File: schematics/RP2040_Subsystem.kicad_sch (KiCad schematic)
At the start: 0 parts

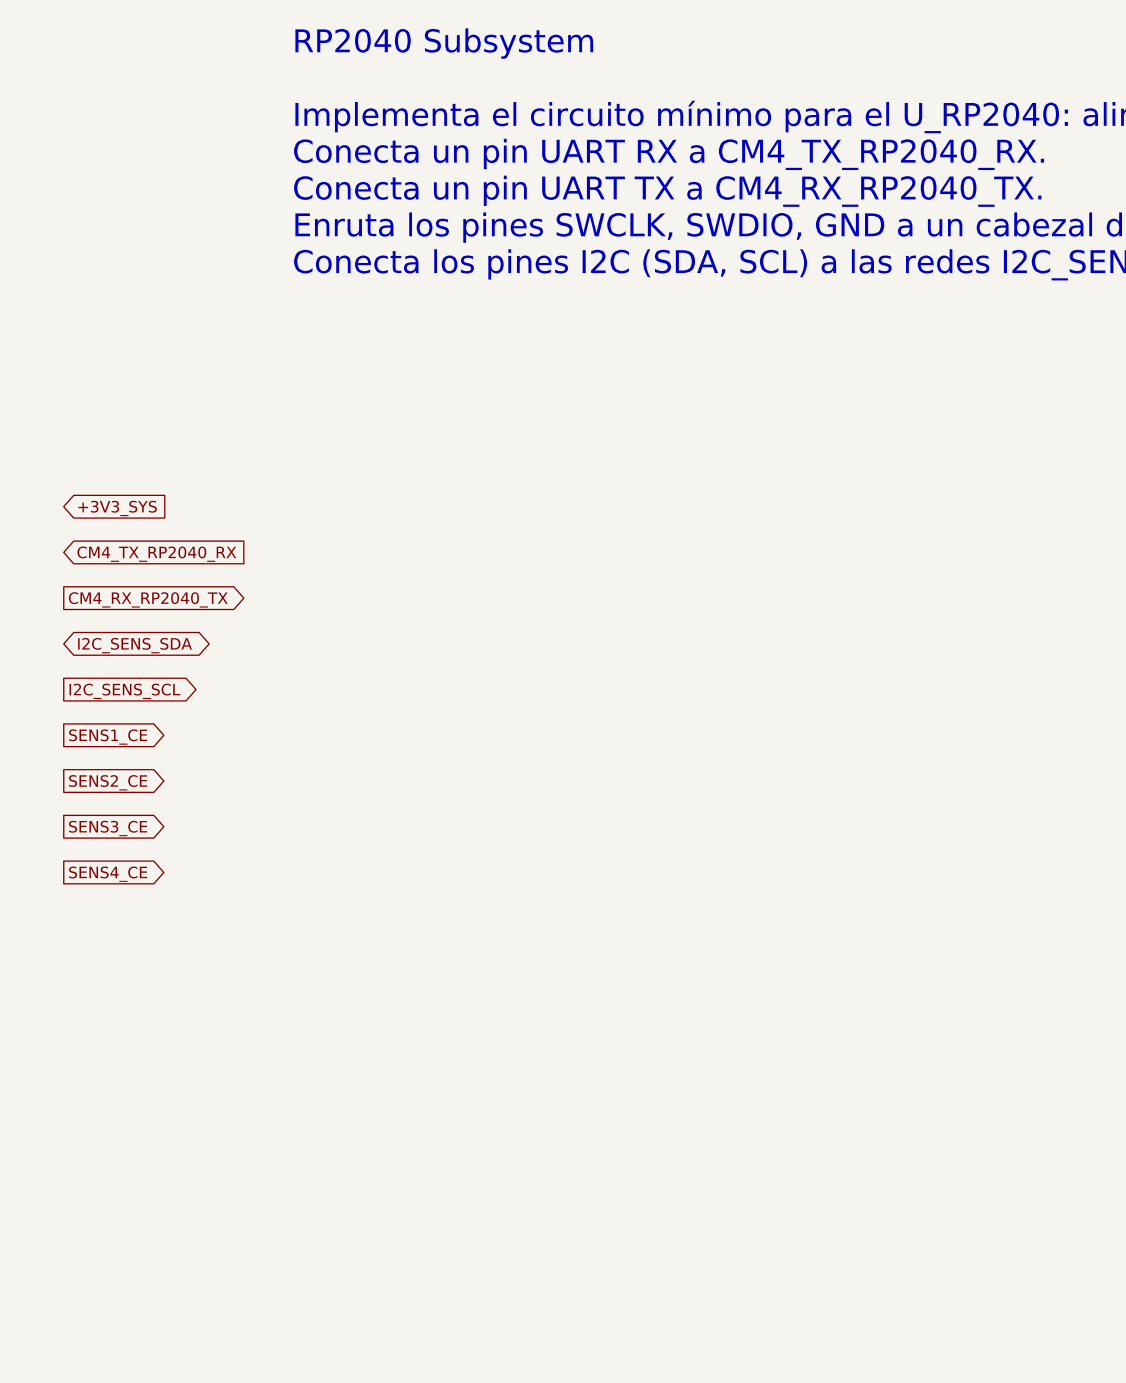
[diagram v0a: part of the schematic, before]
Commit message: Añadir esquemático detallado del subsistema RP2040
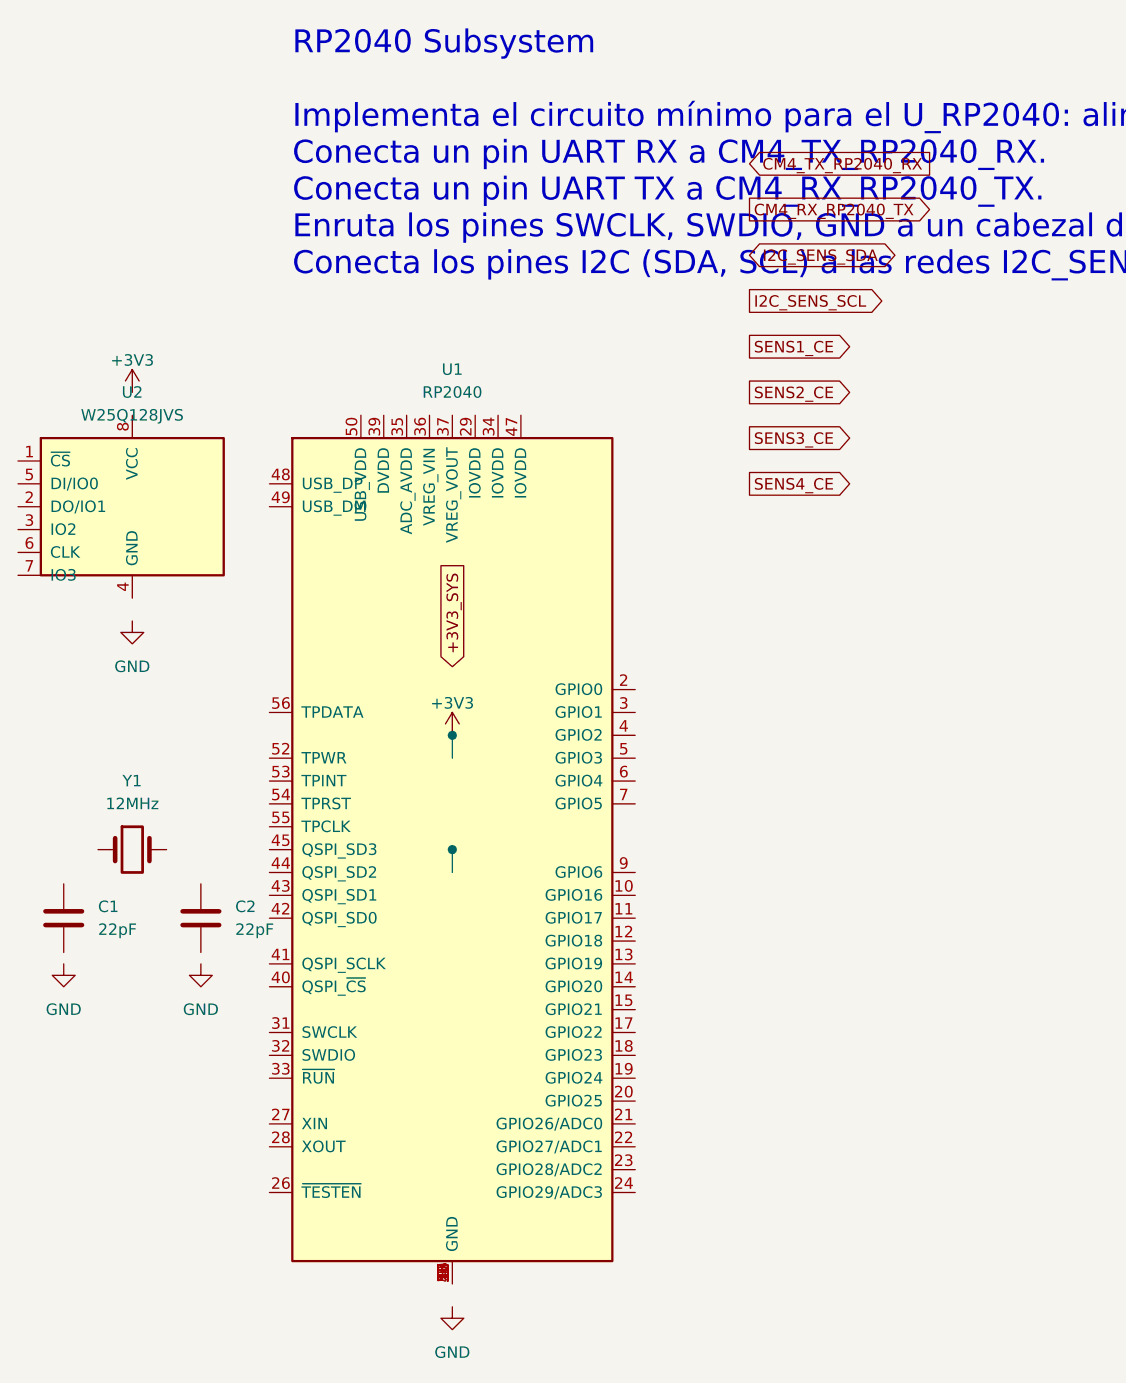
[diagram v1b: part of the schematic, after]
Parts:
- added C1, C2: 22pF, Capacitor_SMD:C_0402_1005Metric, symbol Device:C
- added U1: RP2040, Package_DFN_QFN:QFN-56-1EP_7x7mm_P0.4mm_EP3.2x3.2mm, symbol MCU_RaspberryPi:RP2040
- added U2: W25Q128JVS, Package_SO:SOIC-8_5.23x5.23mm_P1.27mm, symbol Memory_Flash:W25Q128JVS
- added Y1: 12MHz, Crystal:Crystal_SMD_3225-4Pin_3.2x2.5mm, symbol Device:Crystal
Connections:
- new net: U1.1 (GND), U1.16 (GND), U1.25 (GND), U1.30 (GND), U1.38 (GND), U1.46 (GND), U1.51 (GND), U1.57 (GND), U1.8 (GND)
